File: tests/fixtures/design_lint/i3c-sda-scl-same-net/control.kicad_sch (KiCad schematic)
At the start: 1 part, among them U1 I3C controller

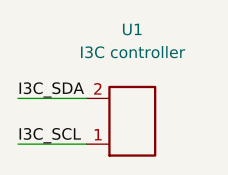
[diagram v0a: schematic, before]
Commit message: fix: align same-net native control fixtures
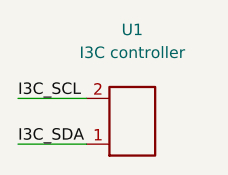
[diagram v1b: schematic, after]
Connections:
- net I3C_SCL: now also U1.2 (I3C1_SCL); no longer U1.1 (I3C1_SDA)
- net I3C_SDA: now also U1.1 (I3C1_SDA); no longer U1.2 (I3C1_SCL)
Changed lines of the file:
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@@
     (pin "1")
     (pin "2")
-    (instances (project "synthetic-i2c-sda-scl-same-net" (path "/8e000000-0000-4000-8000-000000000001" (reference "U1") (unit 1)))))
+    (instances (project "synthetic-i3c-sda-scl-same-net" (path "/8e000000-0000-4000-8000-000000000001" (reference "U1") (unit 1)))))
   (wire (pts (xy 58.42 60.96) (xy 50.80 60.96))
     (stroke (width 0) (type default)))
-  (label "I3C_SDA" (at 50.80 60.96 0)
+  (label "I3C_SCL" (at 50.80 60.96 0)
     (effects (font (size 1.27 1.27)) (justify left bottom))
 )
   (wire (pts (xy 58.42 66.04) (xy 50.80 66.04))
     (stroke (width 0) (type default)))
-  (label "I3C_SCL" (at 50.80 66.04 0)
+  (label "I3C_SDA" (at 50.80 66.04 0)
     (effects (font (size 1.27 1.27)) (justify left bottom))
 )
